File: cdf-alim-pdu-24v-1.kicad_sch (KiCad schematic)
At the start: 0 parts

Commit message: schem: import TPS25983 efuse
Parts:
- added C10: 1n, Capacitor_SMD:C_0603_1608Metric_Pad1.08x0.95mm_HandSolder, symbol Device:C
- added C11, C2: 0u1, Capacitor_SMD:C_0402_1005Metric, symbol Device:C
- added C7: 4n7, Capacitor_SMD:C_0402_1005Metric, symbol Device:C_Small
- added C8: 22n, Capacitor_SMD:C_0402_1005Metric, symbol Device:C
- added D2: SMAJ26CA, Diode_SMD:D_SMA, symbol Device:D_TVS
- added D3: GREEN, LED_SMD:LED_0805_2012Metric, symbol Device:LED
- added D5: SS33, Diode_SMD:D_SMA, symbol Device:D_Schottky
- added J1: Conn_01x02, Connector_AMASS:AMASS_XT30PW-M_1x02_P2.50mm_Horizontal, symbol Connector_Generic:Conn_01x02
- added Q3: BSC019N04LS, Package_TO_SOT_SMD:TDSON-8-1, symbol Transistor_FET:CSD18501Q5A
- added R11: 2, Resistor_SMD:R_0603_1608Metric, symbol Device:R
- added R12: 1k2, Resistor_SMD:R_0603_1608Metric, symbol Device:R_Small
- added R4: 1M, Resistor_SMD:R_0402_1005Metric, symbol Device:R
- added R5: 15k, Resistor_SMD:R_0402_1005Metric, symbol Device:R
- added R6: 49k9, Resistor_SMD:R_0603_1608Metric, symbol Device:R
- added R8: 5k1, Resistor_SMD:R_0402_1005Metric, symbol Device:R
- added R9: 200, Resistor_SMD:R_0402_1005Metric, symbol Device:R
- added TP10, TP3, TP6, TP7: TestPoint, TestPoint:TestPoint_Pad_D2.0mm, symbol Connector:TestPoint
- added U2: TPS25983, GLCS:Texas_RGE0024M_VQFN-24-1EP_4x4mm_P0.5mm_ThermalVias, symbol GLCS:TPS25983
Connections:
- new net: R12.2, TP7.1, U2.9 (IMON)
- new net: R4.2, R5.1, U2.6 (EN/UVLO)
- new net: R5.2, R6.1, U2.12 (OVLO)
- new net: R9.1, U2.8 (ILIM)
- new net: Q3.1 (S), Q3.2 (S), Q3.3 (S), TP6.1, U2.17 (OUT), U2.18 (OUT), U2.19 (OUT), U2.20 (OUT), U2.21 (OUT), U2.22 (OUT), U2.23 (OUT), U2.24 (OUT)
- new net: Q3.4 (G), R11.2
- new net: C11.1, D5.1 (K), Q3.5 (D), TP10.1
- new net: C10.2, R11.1, U2.15 (dVdt/BGATE)
- new net: D3.2 (A), R8.2, U2.13 (PG)
- new net: C8.1, U2.10 (RETRY_DLY)
- new net: C7.1, U2.7 (ITIMER)
- new net +24V: C2.1, D2.1 (A1), J1.2 (Pin_2), R4.1, TP3.1, U2.1 (IN), U2.16 (IN), U2.2 (IN), U2.25 (IN), U2.3 (IN)
- new net +3V3: R8.1
- new net GND: C10.1, C11.2, C2.2, C7.2, C8.2, D2.2 (A2), D3.1 (K), D5.2 (A), J1.1 (Pin_1), R12.1, R6.2, R9.2, U2.11 (NRETRY), U2.14 (GND), U2.26 (GND), U2.4 (GND), U2.5 (GND)
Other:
- note added: "TPS25983 8A 24V Input efuse"

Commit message: schem: add +24V bulk caps
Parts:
- added C26, C27, C28, C29: 10u, Capacitor_SMD:C_1206_3216Metric, symbol Device:C
- added C30, C31, C32, C33: 100u, Capacitor_SMD:CP_Elec_8x10, symbol Device:C_Polarized
- added C34, C35: 220u, Capacitor_SMD:CP_Elec_10x10, symbol Device:C_Polarized
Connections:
- net +24V: now also C11.1, D5.1 (K), Q3.5 (D), TP10.1, C26.1, C27.1, C28.1, C29.1, C30.1, C31.1, C32.1, C33.1, C34.1, C35.1; no longer C2.1, D2.1 (A1), J1.2 (Pin_2), R4.1, TP3.1, U2.1 (IN), U2.16 (IN), U2.2 (IN), U2.25 (IN), U2.3 (IN)
- net GND: now also C26.2, C27.2, C28.2, C29.2, C30.2, C31.2, C32.2, C33.2, C34.2, C35.2
- new net +24V_IN: C2.1, D2.1 (A1), J1.2 (Pin_2), R4.1, TP3.1, U2.1 (IN), U2.16 (IN), U2.2 (IN), U2.25 (IN), U2.3 (IN)

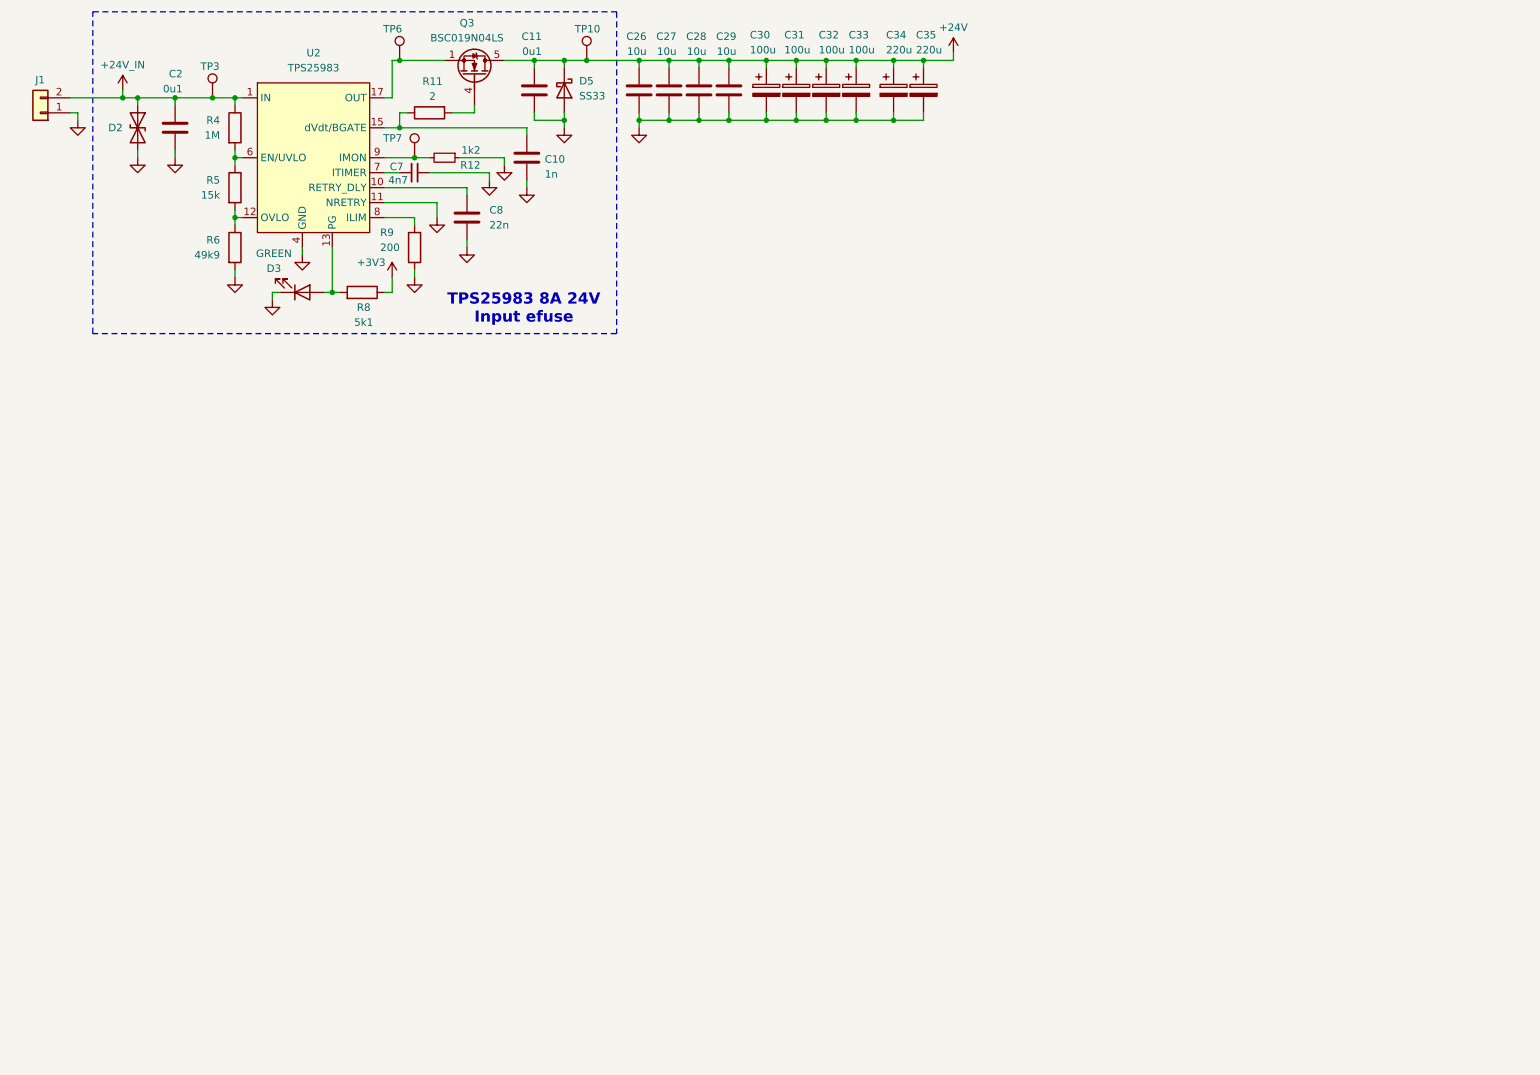
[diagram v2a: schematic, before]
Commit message: schem: add MX25947 24V 2A efuse
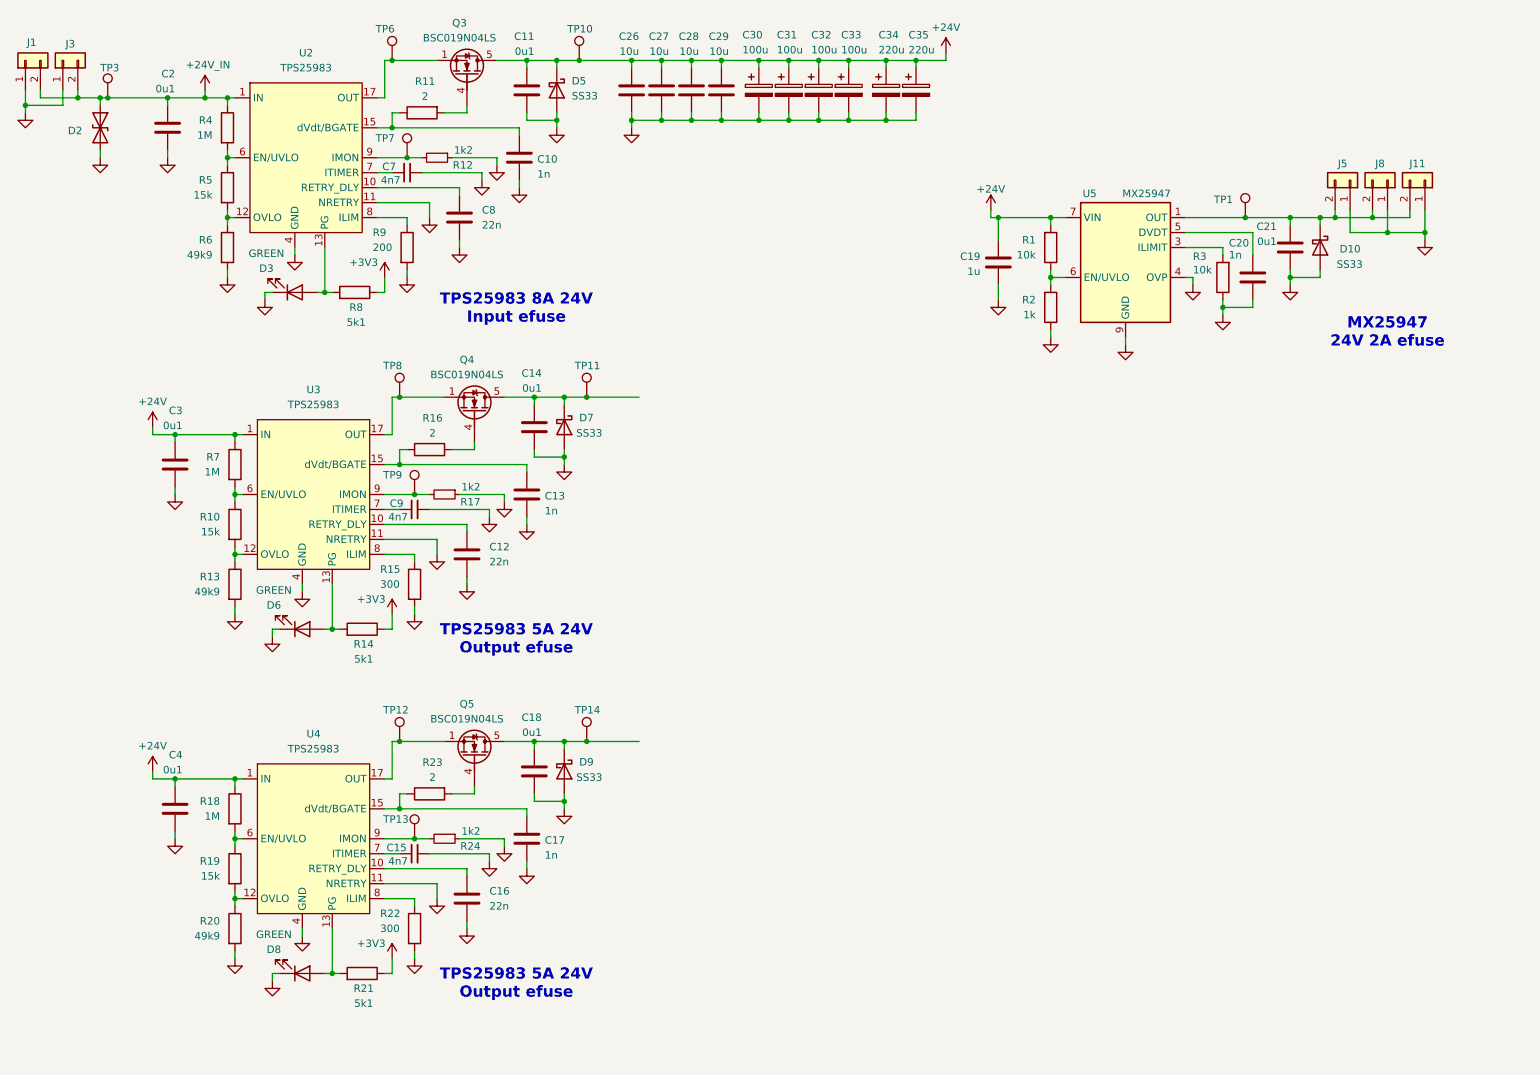
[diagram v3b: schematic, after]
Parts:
- added C12, C16: 22n, Capacitor_SMD:C_0402_1005Metric, symbol Device:C
- added C13, C17: 1n, Capacitor_SMD:C_0603_1608Metric_Pad1.08x0.95mm_HandSolder, symbol Device:C
- added C14, C18, C21, C3, C4: 0u1, Capacitor_SMD:C_0402_1005Metric, symbol Device:C
- added C15, C9: 4n7, Capacitor_SMD:C_0402_1005Metric, symbol Device:C_Small
- added C19: 1u, Capacitor_SMD:C_0402_1005Metric, symbol Device:C
- added C20: 1n, Capacitor_SMD:C_0402_1005Metric, symbol Device:C
- added D10, D7, D9: SS33, Diode_SMD:D_SMA, symbol Device:D_Schottky
- added D6, D8: GREEN, LED_SMD:LED_0805_2012Metric, symbol Device:LED
- added J11, J5, J8: Conn_01x02, Connector_JST:JST_XH_B2B-XH-A_1x02_P2.50mm_Vertical, symbol Connector_Generic:Conn_01x02
- added J3: Conn_01x02, Connector_AMASS:AMASS_XT30PW-F_1x02_P2.50mm_Horizontal, symbol Connector_Generic:Conn_01x02
- added Q4, Q5: BSC019N04LS, Package_TO_SOT_SMD:TDSON-8-1, symbol Transistor_FET:CSD18501Q5A
- added R1, R3: 10k, Resistor_SMD:R_0402_1005Metric, symbol Device:R
- added R10, R19: 15k, Resistor_SMD:R_0402_1005Metric, symbol Device:R
- added R13, R20: 49k9, Resistor_SMD:R_0603_1608Metric, symbol Device:R
- added R14, R21: 5k1, Resistor_SMD:R_0402_1005Metric, symbol Device:R
- added R15, R22: 300, Resistor_SMD:R_0402_1005Metric, symbol Device:R
- added R16, R23: 2, Resistor_SMD:R_0603_1608Metric, symbol Device:R
- added R17, R24: 1k2, Resistor_SMD:R_0603_1608Metric, symbol Device:R_Small
- added R18, R7: 1M, Resistor_SMD:R_0402_1005Metric, symbol Device:R
- added R2: 1k, Resistor_SMD:R_0402_1005Metric, symbol Device:R
- added TP1, TP11, TP12, TP13, TP14, TP8, TP9: TestPoint, TestPoint:TestPoint_Pad_D2.0mm, symbol Connector:TestPoint
- added U3, U4: TPS25983, GLCS:Texas_RGE0024M_VQFN-24-1EP_4x4mm_P0.5mm_ThermalVias, symbol GLCS:TPS25983
- added U5: MX25947, Package_SO:TI_SO-PowerPAD-8_ThermalVias, symbol GLCS:MX25947
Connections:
- net +24V_IN is gone; now on net +24V: C2.1, D2.1 (A1), J1.2 (Pin_2), R4.1, TP3.1, U2.1 (IN), U2.16 (IN), U2.2 (IN), U2.25 (IN), U2.3 (IN)
- net +24V: now also C19.2, C3.1, C4.1, J3.2 (Pin_2), R1.2, R18.1, R7.1, U3.1 (IN), U3.16 (IN), U3.2 (IN), U3.25 (IN), U3.3 (IN), U4.1 (IN), U4.16 (IN), U4.2 (IN), U4.25 (IN), U4.3 (IN), U5.7 (VIN), U5.8 (VIN)
- net +3V3: now also R14.1, R21.1
- net GND: now also C12.2, C13.1, C14.2, C15.2, C16.2, C17.1, C18.2, C19.1, C20.2, C21.2, C3.2, C4.2, C9.2, D10.2 (A), D6.1 (K), D7.2 (A), D8.1 (K), D9.2 (A), J11.1 (Pin_1), J3.1 (Pin_1), J5.1 (Pin_1), J8.1 (Pin_1), R13.2, R15.2, R17.1, R2.1, R20.2, R22.2, R24.1, R3.1, U3.11 (NRETRY), U3.14 (GND), U3.26 (GND), U3.4 (GND), U3.5 (GND), U4.11 (NRETRY), U4.14 (GND), U4.26 (GND), U4.4 (GND), U4.5 (GND), U5.4 (OVP), U5.9 (GND)
- new net: R17.2, TP9.1, U3.9 (IMON)
- new net: R24.2, TP13.1, U4.9 (IMON)
- new net: C14.1, D7.1 (K), Q4.5 (D), TP11.1
- new net: C13.2, R16.1, U3.15 (dVdt/BGATE)
- new net: Q4.4 (G), R16.2
- new net: D6.2 (A), R14.2, U3.13 (PG)
- new net: C12.1, U3.10 (RETRY_DLY)
- new net: R10.2, R13.1, U3.12 (OVLO)
- new net: Q4.1 (S), Q4.2 (S), Q4.3 (S), TP8.1, U3.17 (OUT), U3.18 (OUT), U3.19 (OUT), U3.20 (OUT), U3.21 (OUT), U3.22 (OUT), U3.23 (OUT), U3.24 (OUT)
- new net: R10.1, R7.2, U3.6 (EN/UVLO)
- new net: C9.1, U3.7 (ITIMER)
- new net: R15.1, U3.8 (ILIM)
- new net: R1.1, R2.2, U5.6 (EN/UVLO)
- new net: R19.2, R20.1, U4.12 (OVLO)
- new net: C21.1, D10.1 (K), J11.2 (Pin_2), J5.2 (Pin_2), J8.2 (Pin_2), TP1.1, U5.1 (OUT), U5.2 (OUT)
- new net: R3.2, U5.3 (ILIMIT)
- new net: C20.1, U5.5 (DVDT)
- new net: C16.1, U4.10 (RETRY_DLY)
- new net: D8.2 (A), R21.2, U4.13 (PG)
- new net: C17.2, R23.1, U4.15 (dVdt/BGATE)
- new net: Q5.1 (S), Q5.2 (S), Q5.3 (S), TP12.1, U4.17 (OUT), U4.18 (OUT), U4.19 (OUT), U4.20 (OUT), U4.21 (OUT), U4.22 (OUT), U4.23 (OUT), U4.24 (OUT)
- new net: R18.2, R19.1, U4.6 (EN/UVLO)
- new net: C15.1, U4.7 (ITIMER)
- new net: R22.1, U4.8 (ILIM)
- new net: C18.1, D9.1 (K), Q5.5 (D), TP14.1
- new net: Q5.4 (G), R23.2
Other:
- note added: "MX25947 24V 2A efuse"
- note added: "TPS25983 5A 24V Output efuse"
- moved on the sheet: C10, C11, C2, C26, C27, C28, C29, C30, C31, C32, C33, C34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

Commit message: schem: add all output power connectors
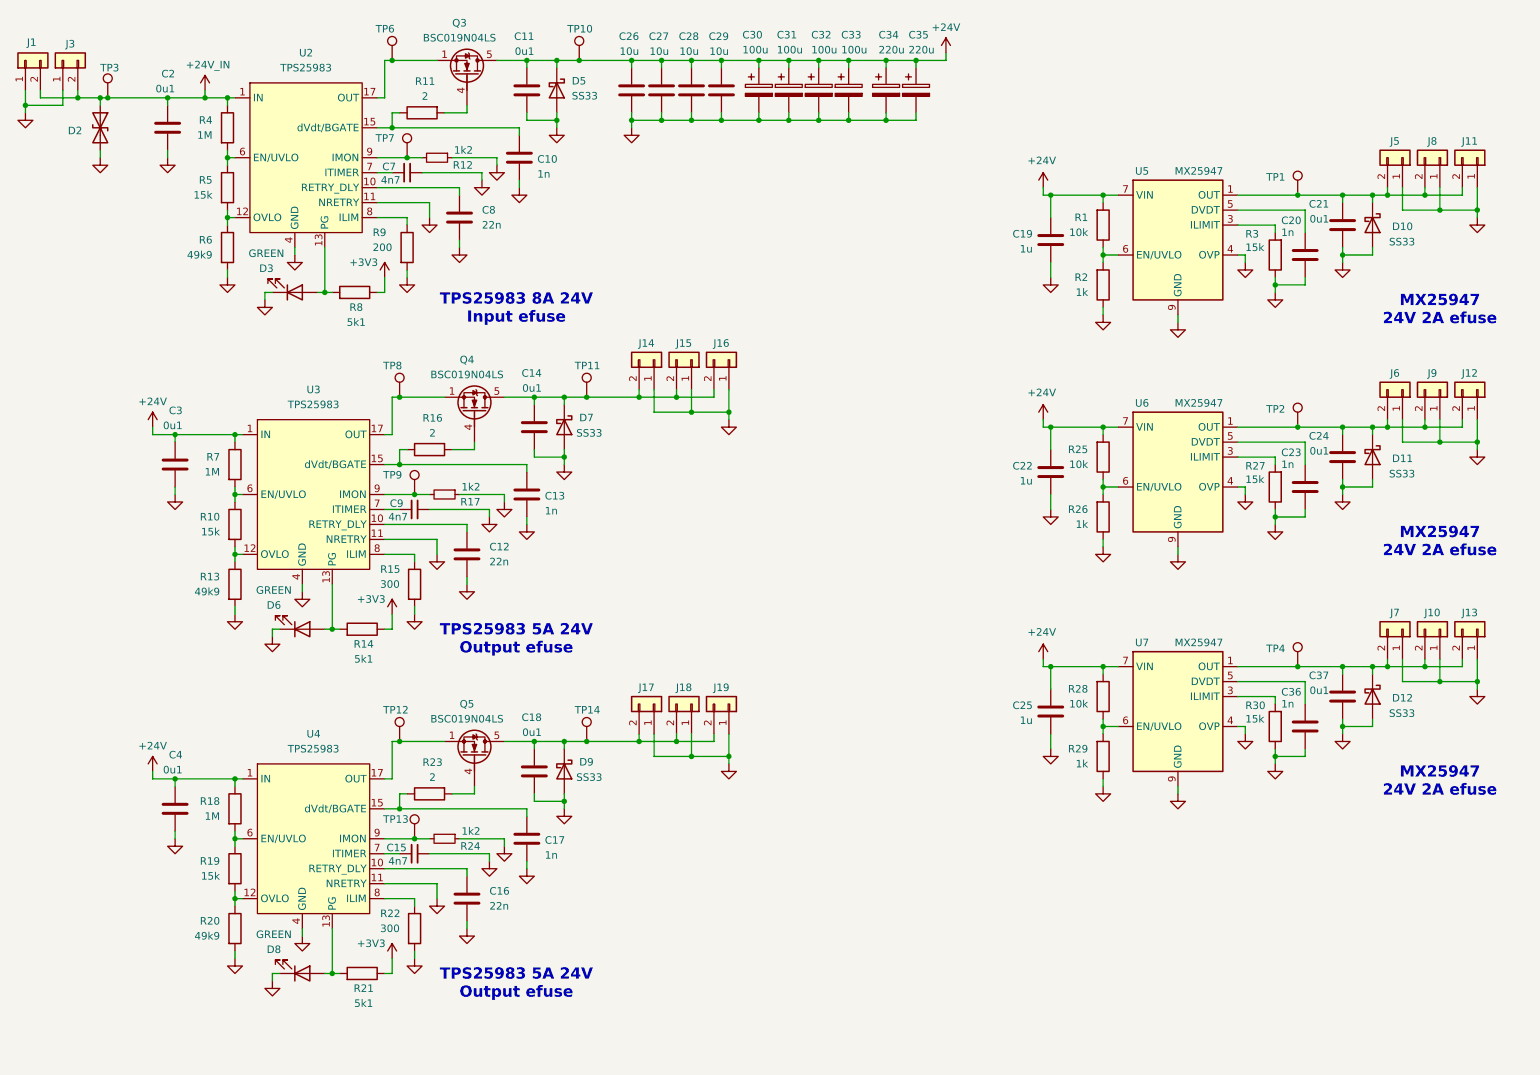
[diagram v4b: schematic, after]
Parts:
- added C22, C25: 1u, Capacitor_SMD:C_0402_1005Metric, symbol Device:C
- added C23, C36: 1n, Capacitor_SMD:C_0402_1005Metric, symbol Device:C
- added C24, C37: 0u1, Capacitor_SMD:C_0402_1005Metric, symbol Device:C
- added D11, D12: SS33, Diode_SMD:D_SMA, symbol Device:D_Schottky
- added J10, J12, J13, J14, J15, J16, J17, J18, J19, J6, J7, J9: Conn_01x02, Connector_JST:JST_XH_B2B-XH-A_1x02_P2.50mm_Vertical, symbol Connector_Generic:Conn_01x02
- added R25, R28: 10k, Resistor_SMD:R_0402_1005Metric, symbol Device:R
- added R26, R29: 1k, Resistor_SMD:R_0402_1005Metric, symbol Device:R
- added R27, R30: 15k, Resistor_SMD:R_0402_1005Metric, symbol Device:R
- added TP2, TP4: TestPoint, TestPoint:TestPoint_Pad_D2.0mm, symbol Connector:TestPoint
- added U6, U7: MX25947, Package_SO:TI_SO-PowerPAD-8_ThermalVias, symbol GLCS:MX25947
- R3: value 10k -> 15k; JLCPCB Part # C25744 -> C25756; Manufacturer Part Number 0402WGF1002TCE -> 0402WGF1502TCE
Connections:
- net +24V: now also C22.2, C25.2, R25.2, R28.2, U6.7 (VIN), U6.8 (VIN), U7.7 (VIN), U7.8 (VIN)
- net GND: now also C22.1, C23.2, C24.2, C25.1, C36.2, C37.2, D11.2 (A), D12.2 (A), J10.1 (Pin_1), J12.1 (Pin_1), J13.1 (Pin_1), J14.1 (Pin_1), J15.1 (Pin_1), J16.1 (Pin_1), J17.1 (Pin_1), J18.1 (Pin_1), J19.1 (Pin_1), J6.1 (Pin_1), J7.1 (Pin_1), J9.1 (Pin_1), R26.1, R27.1, R29.1, R30.1, U6.4 (OVP), U6.9 (GND), U7.4 (OVP), U7.9 (GND)
- net at C14.1, D7.1 (K), Q4.5 (D)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: now also J14.2 (Pin_2), J15.2 (Pin_2), J16.2 (Pin_2)
- net at C18.1, D9.1 (K), Q5.5 (D)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: now also J17.2 (Pin_2), J18.2 (Pin_2), J19.2 (Pin_2)
- new net: C36.1, U7.5 (DVDT)
- new net: C24.1, D11.1 (K), J12.2 (Pin_2), J6.2 (Pin_2), J9.2 (Pin_2), TP2.1, U6.1 (OUT), U6.2 (OUT)
- new net: C37.1, D12.1 (K), J10.2 (Pin_2), J13.2 (Pin_2), J7.2 (Pin_2), TP4.1, U7.1 (OUT), U7.2 (OUT)
- new net: R30.2, U7.3 (ILIMIT)
- new net: R25.1, R26.2, U6.6 (EN/UVLO)
- new net: R28.1, R29.2, U7.6 (EN/UVLO)
- new net: C23.1, U6.5 (DVDT)
- new net: R27.2, U6.3 (ILIMIT)
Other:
- moved on the sheet: C19, C20, C21, D10, J11, J5, J8, R1, R2, R3, TP1, U5

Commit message: schem: add 2A efuses output leds
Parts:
- added D13, D14, D4: YELLOW, LED_SMD:LED_0805_2012Metric, symbol Device:LED
- added R31, R32, R33: 10k, Resistor_SMD:R_0402_1005Metric, symbol Device:R
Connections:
- net GND: now also R31.2, R32.2, R33.2
- net at C24.1, D11.1 (K), J12.2 (Pin_2)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: now also D13.2 (A)
- net at C37.1, D12.1 (K), J10.2 (Pin_2)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: now also D4.2 (A)
- net at C21.1, D10.1 (K), J11.2 (Pin_2)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: now also D14.2 (A)
- new net: D4.1 (K), R31.1
- new net: D14.1 (K), R33.1
- new net: D13.1 (K), R32.1

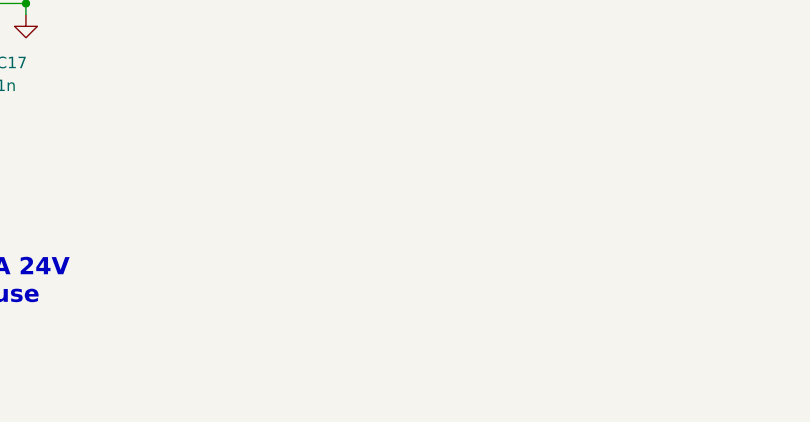
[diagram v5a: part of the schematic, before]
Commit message: schem: add +3V3 ldo
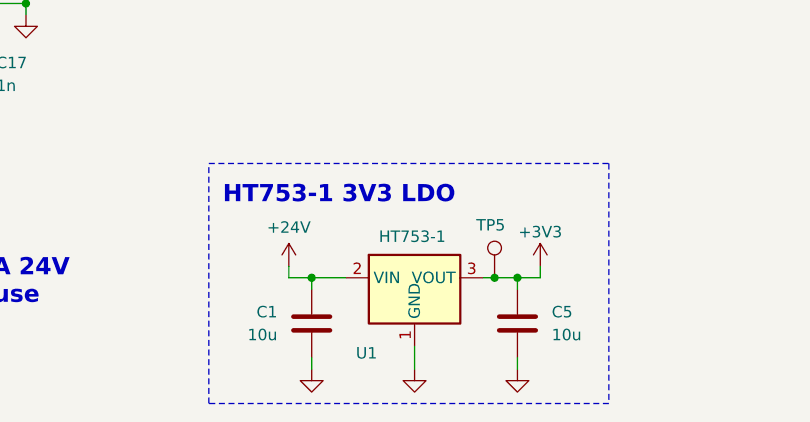
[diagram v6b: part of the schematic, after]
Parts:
- added C1, C5: 10u, Capacitor_SMD:C_0805_2012Metric, symbol Device:C
- added TP5: TestPoint, TestPoint:TestPoint_Pad_D2.0mm, symbol Connector:TestPoint
- added U1: HT753-1, Package_TO_SOT_SMD:SOT-89-3, symbol Regulator_Linear:HT75xx-1-SOT89
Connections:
- net +24V: now also C1.1, U1.2 (VIN)
- net +3V3: now also C5.1, TP5.1, U1.3 (VOUT)
- net GND: now also C1.2, C5.2, U1.1 (GND)
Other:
- note added: "HT753-1 3V3 LDO"
